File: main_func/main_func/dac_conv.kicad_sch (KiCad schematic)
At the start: 38 parts, among them U1 TXB0108PWR, U2 DRV603PW, U3 SN74AHC1G14DCKR, U4 PCM1753DBQR

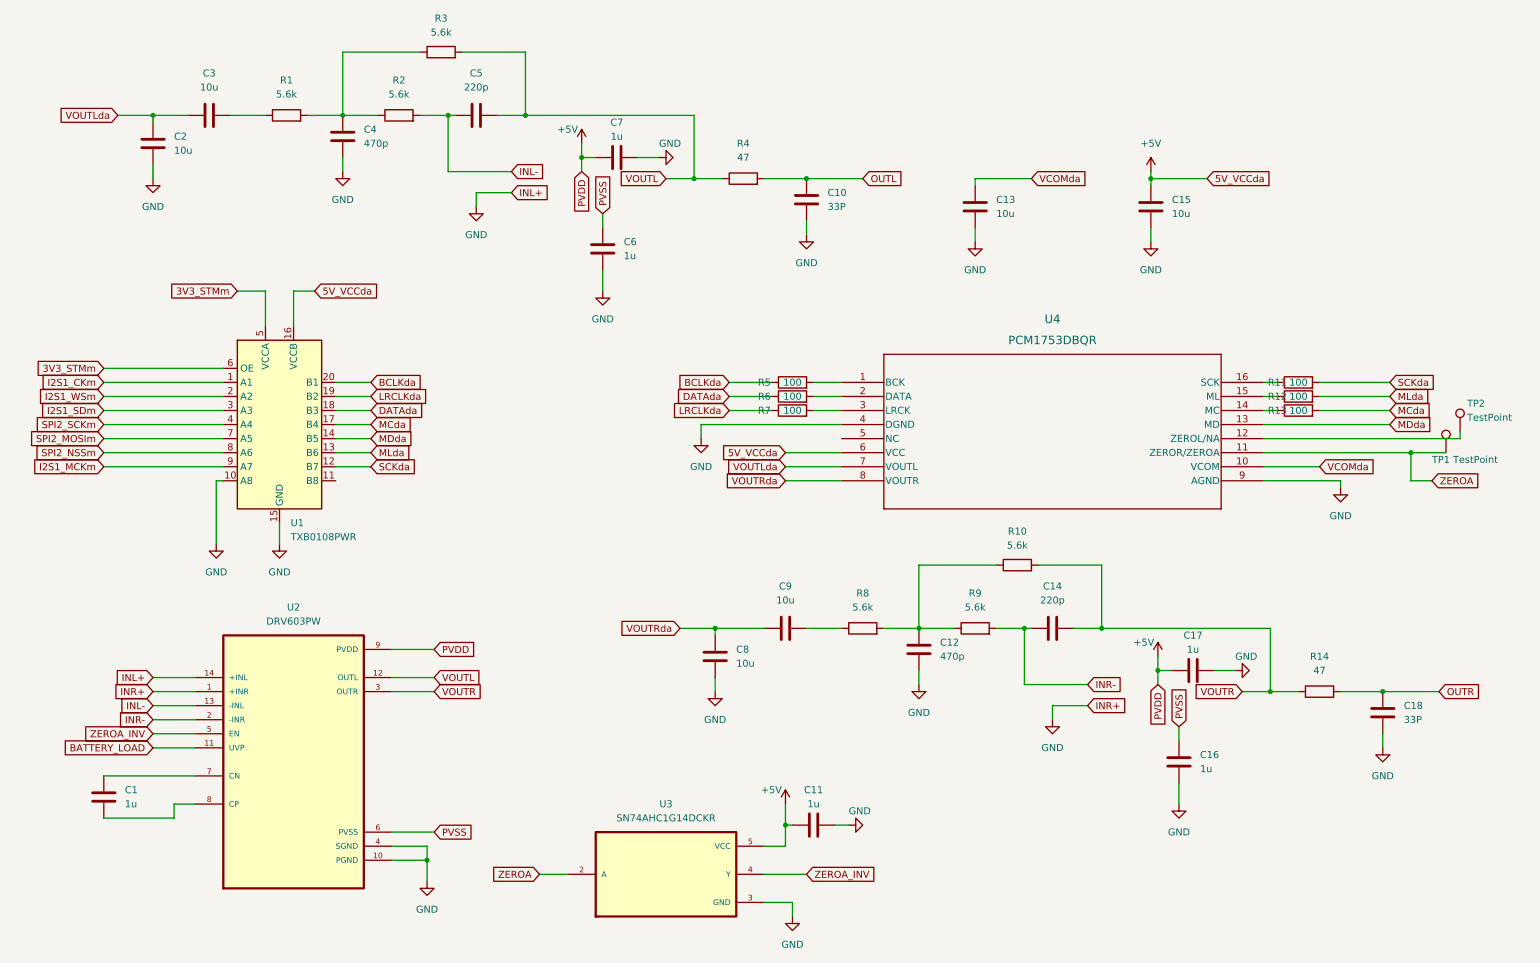
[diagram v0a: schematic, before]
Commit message: main func schematics fixed
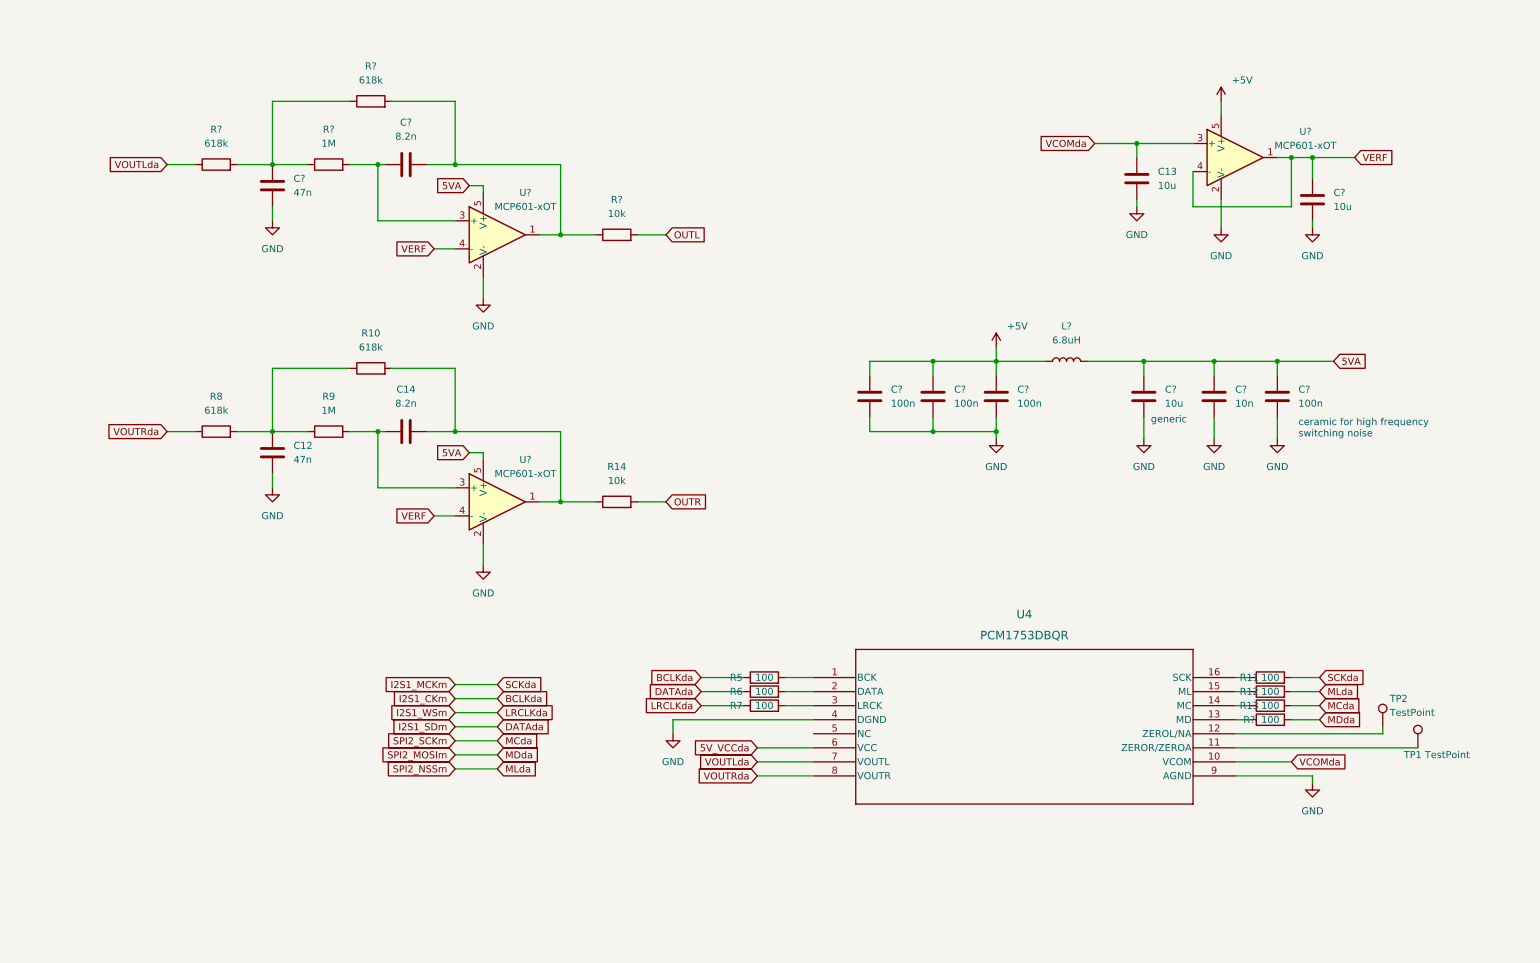
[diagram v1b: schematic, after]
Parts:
- removed C1, C11, C16, C17, C6, C7: 1u, Capacitor_SMD:C_0805_2012Metric_Pad1.18x1.45mm_HandSolder, symbol Device:C
- removed C10, C18: 33P, Capacitor_SMD:C_0805_2012Metric_Pad1.18x1.45mm_HandSolder, symbol Device:C
- removed C15, C2, C3, C8, C9: 10u, Capacitor_SMD:C_0805_2012Metric_Pad1.18x1.45mm_HandSolder, symbol Device:C
- removed C4: 470p, Capacitor_SMD:C_0805_2012Metric_Pad1.18x1.45mm_HandSolder, symbol Device:C
- removed C5: 220p, Capacitor_SMD:C_0805_2012Metric_Pad1.18x1.45mm_HandSolder, symbol Device:C
- removed R1, R2, R3: 5.6k, Resistor_SMD:R_0805_2012Metric_Pad1.20x1.40mm_HandSolder, symbol Device:R
- removed R4: 47, Resistor_SMD:R_0805_2012Metric_Pad1.20x1.40mm_HandSolder, symbol Device:R
- removed U1: TXB0108PWR, Package_SO:TSSOP-20_4.4x6.5mm_P0.65mm, symbol Logic_LevelTranslator:TXB0108DQSR
- removed U2: DRV603PW, DRV603PW:SOP65P640X120-14N, symbol DRV603PW:DRV603PW
- removed U3: SN74AHC1G14DCKR, SN74AHC1G14DCKR:SOT65P210X110-5N, symbol SN74AHC1G14DCKR:SN74AHC1G14DCKR
- added C?: 10n, Capacitor_SMD:C_0805_2012Metric_Pad1.18x1.45mm_HandSolder, symbol Device:C
- added C? (x4): 100n, Capacitor_SMD:C_0805_2012Metric_Pad1.18x1.45mm_HandSolder, symbol Device:C
- added C? (x2): 10u, Capacitor_SMD:C_0805_2012Metric_Pad1.18x1.45mm_HandSolder, symbol Device:C
- added C?: 47n, Capacitor_SMD:C_0805_2012Metric_Pad1.18x1.45mm_HandSolder, symbol Device:C
- added C?: 8.2n, Capacitor_SMD:C_0805_2012Metric_Pad1.18x1.45mm_HandSolder, symbol Device:C
- added L?: 6.8uH, inductors:inductor_koherelec, symbol Device:L
- added R?: 100, Resistor_SMD:R_0805_2012Metric_Pad1.20x1.40mm_HandSolder, symbol Device:R
- added R? (x2): 618k, Resistor_SMD:R_0805_2012Metric_Pad1.20x1.40mm_HandSolder, symbol Device:R
- added R?: 1M, Resistor_SMD:R_0805_2012Metric_Pad1.20x1.40mm_HandSolder, symbol Device:R
- added R?: 10k, Resistor_SMD:R_0805_2012Metric_Pad1.20x1.40mm_HandSolder, symbol Device:R
- added U? (x3): MCP601-xOT, Package_TO_SOT_SMD:SOT-23-5, symbol Amplifier_Operational:MCP601-xOT
- C12: value 470p -> 47n
- C14: value 220p -> 8.2n
- R10, R8: value 5.6k -> 618k
- R14: value 47 -> 10k
- R9: value 5.6k -> 1M
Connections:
- net LRCLKda is gone; now on net I2S1_WSm: R7.1
- net SCKda is gone; now on net I2S1_MCKm: R11.2
- net +5V: now also C?.1, C?.1, C?.1, L?.1, U?.5 (V+); no longer U4.6 (VCC)
- net GND: now also C?.2, C?.2, C?.2, C?.2, C?.2, C?.2, C?.2, C?.2, U?.2 (V-), U?.2 (V-), U?.2 (V-)
- net MDda: now also R?.2; no longer U4.13 (MD)
- net OUTL: now also R?.2
- net VCOMda: now also U?.3 (+)
- net VOUTLda: now also R?.1
- net VOUTRda: now also R8.1
- net INR-: no longer names the net of C14.1, R9.2
- net INR-: now also U?.3 (+)
- net VOUTR: no longer names the net of C14.2, R10.2, R14.1
- net VOUTR: now also U?.1
- net ZEROA: no longer names the net of TP1.1, U4.11 (ZEROR/ZEROA)
- new net: C?.2, R?.1, R?.2, U?.1
- new net: C?.1, R?.2, U?.3 (+)
- new net: R?.1, U4.13 (MD)
- new net: C?.1, R?.1, R?.1, R?.2
- new net 5VA: C?.1, C?.1, C?.1, L?.2, U?.5 (V+), U?.5 (V+)
- new net 5V_VCCda: U4.6 (VCC)
- new net VERF: C?.1, U?.1, U?.4 (-), U?.4 (-), U?.4 (-)
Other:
- note added: "ceramic for high frequency switching noise"
- note added: "generic"
- moved on the sheet: C12, C13, C14, R10, R11, R12, R13, R14, R5, R6, R7, R8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

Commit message: fixing keyboard and pot project schematics
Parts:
- gave numbers to parts that had none: 18
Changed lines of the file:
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@@
   (symbol (lib_id "Amplifier_Operational:MCP601-xOT") (at 100.33 49.53 0) (unit 1)
     (in_bom yes) (on_board yes)
-    (property "Reference" "U?" (id 0) (at 105.41 41.91 0))
+    (property "Reference" "U1" (id 0) (at 105.41 41.91 0))
     (property "Value" "MCP601-xOT" (id 1) (at 105.41 44.45 0))
     (property "Footprint" "Package_TO_SOT_SMD:SOT-23-5" (id 2) (at 97.79 54.61 0)
@@
   (symbol (lib_id "Device:C") (at 229.87 78.74 0) (unit 1)
     (in_bom yes) (on_board yes) (fields_autoplaced)
-    (property "Reference" "C?" (id 0) (at 233.68 77.4699 0)
+    (property "Reference" "C7" (id 0) (at 233.68 77.4699 0)
       (effects (font (size 1.27 1.27)) (justify left))
     )
@@
   (symbol (lib_id "Device:C") (at 241.3 78.74 0) (unit 1)
     (in_bom yes) (on_board yes) (fields_autoplaced)
-    (property "Reference" "C?" (id 0) (at 245.11 77.4699 0)
+    (property "Reference" "C8" (id 0) (at 245.11 77.4699 0)
       (effects (font (size 1.27 1.27)) (justify left))
     )
@@
   (symbol (lib_id "power:GND") (at 231.14 48.26 0) (unit 1)
     (in_bom yes) (on_board yes) (fields_autoplaced)
-    (property "Reference" "#PWR?" (id 0) (at 231.14 54.61 0)
+    (property "Reference" "#PWR08" (id 0) (at 231.14 54.61 0)
       (effects (font (size 1.27 1.27)) hide)
     )
@@
   (symbol (lib_id "Device:C") (at 217.17 78.74 0) (unit 1)
     (in_bom yes) (on_board yes) (fields_autoplaced)
-    (property "Reference" "C?" (id 0) (at 220.98 77.4699 0)
+    (property "Reference" "C6" (id 0) (at 220.98 77.4699 0)
       (effects (font (size 1.27 1.27)) (justify left))
     )
@@
   (symbol (lib_id "Device:R") (at 240.03 137.16 90) (unit 1)
     (in_bom yes) (on_board yes)
-    (property "Reference" "R?" (id 0) (at 236.22 137.16 90))
+    (property "Reference" "R28" (id 0) (at 236.22 137.16 90))
     (property "Value" "100" (id 1) (at 240.03 137.16 90))
     (property "Footprint" "Resistor_SMD:R_0805_2012Metric_Pad1.20x1.40mm_HandSolder" (id 2) (at 240.03 138.938 90)
@@
   (symbol (lib_id "power:GND") (at 247.65 48.26 0) (unit 1)
     (in_bom yes) (on_board yes) (fields_autoplaced)
-    (property "Reference" "#PWR?" (id 0) (at 247.65 54.61 0)
+    (property "Reference" "#PWR011" (id 0) (at 247.65 54.61 0)
       (effects (font (size 1.27 1.27)) hide)
     )
@@
   (symbol (lib_id "Device:C") (at 59.69 40.64 0) (unit 1)
     (in_bom yes) (on_board yes) (fields_autoplaced)
-    (property "Reference" "C?" (id 0) (at 63.5 39.3699 0)
+    (property "Reference" "C1" (id 0) (at 63.5 39.3699 0)
       (effects (font (size 1.27 1.27)) (justify left))
     )
@@
   (symbol (lib_id "power:GND") (at 217.17 86.36 0) (unit 1)
     (in_bom yes) (on_board yes) (fields_autoplaced)
-    (property "Reference" "#PWR?" (id 0) (at 217.17 92.71 0)
+    (property "Reference" "#PWR05" (id 0) (at 217.17 92.71 0)
       (effects (font (size 1.27 1.27)) hide)
     )
@@
   (symbol (lib_id "Device:C") (at 167.64 78.74 0) (unit 1)
     (in_bom yes) (on_board yes) (fields_autoplaced)
-    (property "Reference" "C?" (id 0) (at 171.45 77.4699 0)
+    (property "Reference" "C3" (id 0) (at 171.45 77.4699 0)
       (effects (font (size 1.27 1.27)) (justify left))
     )
@@
   (symbol (lib_id "power:GND") (at 59.69 46.99 0) (unit 1)
     (in_bom yes) (on_board yes) (fields_autoplaced)
-    (property "Reference" "#PWR?" (id 0) (at 59.69 53.34 0)
+    (property "Reference" "#PWR01" (id 0) (at 59.69 53.34 0)
       (effects (font (size 1.27 1.27)) hide)
     )
@@
   (symbol (lib_id "Device:C") (at 190.5 78.74 0) (unit 1)
     (in_bom yes) (on_board yes) (fields_autoplaced)
-    (property "Reference" "C?" (id 0) (at 194.31 77.4699 0)
+    (property "Reference" "C5" (id 0) (at 194.31 77.4699 0)
       (effects (font (size 1.27 1.27)) (justify left))
     )
@@
   (symbol (lib_id "power:GND") (at 190.5 86.36 0) (unit 1)
     (in_bom yes) (on_board yes) (fields_autoplaced)
-    (property "Reference" "#PWR?" (id 0) (at 190.5 92.71 0)
+    (property "Reference" "#PWR04" (id 0) (at 190.5 92.71 0)
       (effects (font (size 1.27 1.27)) hide)
     )
@@
   (symbol (lib_id "Amplifier_Operational:MCP601-xOT") (at 233.68 35.56 0) (unit 1)
     (in_bom yes) (on_board yes) (fields_autoplaced)
-    (property "Reference" "U?" (id 0) (at 246.38 30.861 0))
+    (property "Reference" "U3" (id 0) (at 246.38 30.861 0))
     (property "Value" "MCP601-xOT" (id 1) (at 246.38 33.401 0))
     (property "Footprint" "Package_TO_SOT_SMD:SOT-23-5" (id 2) (at 231.14 40.64 0)
@@
   (symbol (lib_id "Device:R") (at 77.47 25.4 90) (unit 1)
     (in_bom yes) (on_board yes) (fields_autoplaced)
-    (property "Reference" "R?" (id 0) (at 77.47 19.05 90))
+    (property "Reference" "R3" (id 0) (at 77.47 19.05 90))
     (property "Value" "618k" (id 1) (at 77.47 21.59 90))
     (property "Footprint" "Resistor_SMD:R_0805_2012Metric_Pad1.20x1.40mm_HandSolder" (id 2) (at 77.47 27.178 90)
@@
   (symbol (lib_id "power:GND") (at 241.3 86.36 0) (unit 1)
     (in_bom yes) (on_board yes) (fields_autoplaced)
-    (property "Reference" "#PWR?" (id 0) (at 241.3 92.71 0)
+    (property "Reference" "#PWR09" (id 0) (at 241.3 92.71 0)
       (effects (font (size 1.27 1.27)) hide)
     )
@@
   (symbol (lib_id "power:+5V") (at 231.14 25.4 0) (unit 1)
     (in_bom yes) (on_board yes)
-    (property "Reference" "#PWR?" (id 0) (at 231.14 29.21 0)
+    (property "Reference" "#PWR07" (id 0) (at 231.14 29.21 0)
       (effects (font (size 1.27 1.27)) hide)
     )
@@
   (symbol (lib_id "Device:R") (at 49.53 36.83 90) (unit 1)
     (in_bom yes) (on_board yes) (fields_autoplaced)
-    (property "Reference" "R?" (id 0) (at 49.53 30.48 90))
+    (property "Reference" "R1" (id 0) (at 49.53 30.48 90))
     (property "Value" "618k" (id 1) (at 49.53 33.02 90))
     (property "Footprint" "Resistor_SMD:R_0805_2012Metric_Pad1.20x1.40mm_HandSolder" (id 2) (at 49.53 38.608 90)
@@
   (symbol (lib_id "Device:C") (at 179.07 78.74 0) (unit 1)
     (in_bom yes) (on_board yes) (fields_autoplaced)
-    (property "Reference" "C?" (id 0) (at 182.88 77.4699 0)
+    (property "Reference" "C4" (id 0) (at 182.88 77.4699 0)
       (effects (font (size 1.27 1.27)) (justify left))
     )
@@
   (symbol (lib_id "Device:C") (at 83.82 36.83 90) (unit 1)
     (in_bom yes) (on_board yes) (fields_autoplaced)
-    (property "Reference" "C?" (id 0) (at 83.82 29.21 90))
+    (property "Reference" "C2" (id 0) (at 83.82 29.21 90))
     (property "Value" "8.2n" (id 1) (at 83.82 31.75 90))
     (property "Footprint" "Capacitor_SMD:C_0805_2012Metric_Pad1.18x1.45mm_HandSolder" (id 2) (at 87.63 35.8648 0)
@@
   (symbol (lib_id "Amplifier_Operational:MCP601-xOT") (at 100.33 97.79 0) (unit 1)
     (in_bom yes) (on_board yes)
-    (property "Reference" "U?" (id 0) (at 105.41 90.17 0))
+    (property "Reference" "U2" (id 0) (at 105.41 90.17 0))
     (property "Value" "MCP601-xOT" (id 1) (at 105.41 92.71 0))
     (property "Footprint" "Package_TO_SOT_SMD:SOT-23-5" (id 2) (at 97.79 102.87 0)
@@
   (symbol (lib_id "power:+5V") (at 190.5 69.85 0) (unit 1)
     (in_bom yes) (on_board yes)
-    (property "Reference" "#PWR?" (id 0) (at 190.5 73.66 0)
+    (property "Reference" "#PWR03" (id 0) (at 190.5 73.66 0)
       (effects (font (size 1.27 1.27)) hide)
     )
@@
   (symbol (lib_id "Device:L") (at 203.2 72.39 90) (unit 1)
     (in_bom yes) (on_board yes) (fields_autoplaced)
-    (property "Reference" "L?" (id 0) (at 203.2 66.04 90))
+    (property "Reference" "L1" (id 0) (at 203.2 66.04 90))
     (property "Value" "6.8uH" (id 1) (at 203.2 68.58 90))
     (property "Footprint" "inductors:inductor_koherelec" (id 2) (at 203.2 72.39 0)
@@
   (symbol (lib_id "Device:R") (at 69.85 36.83 90) (unit 1)
     (in_bom yes) (on_board yes) (fields_autoplaced)
-    (property "Reference" "R?" (id 0) (at 69.85 30.48 90))
+    (property "Reference" "R2" (id 0) (at 69.85 30.48 90))
     (property "Value" "1M" (id 1) (at 69.85 33.02 90))
     (property "Footprint" "Resistor_SMD:R_0805_2012Metric_Pad1.20x1.40mm_HandSolder" (id 2) (at 69.85 38.608 90)
@@
   (symbol (lib_id "power:GND") (at 229.87 86.36 0) (unit 1)
     (in_bom yes) (on_board yes) (fields_autoplaced)
-    (property "Reference" "#PWR?" (id 0) (at 229.87 92.71 0)
+    (property "Reference" "#PWR06" (id 0) (at 229.87 92.71 0)
       (effects (font (size 1.27 1.27)) hide)
     )
@@
   (symbol (lib_id "power:GND") (at 97.79 60.96 0) (unit 1)
     (in_bom yes) (on_board yes) (fields_autoplaced)
-    (property "Reference" "#PWR?" (id 0) (at 97.79 67.31 0)
+    (property "Reference" "#PWR02" (id 0) (at 97.79 67.31 0)
       (effects (font (size 1.27 1.27)) hide)
     )
@@
   (symbol (lib_id "Device:C") (at 247.65 43.18 0) (unit 1)
     (in_bom yes) (on_board yes) (fields_autoplaced)
-    (property "Reference" "C?" (id 0) (at 251.46 41.9099 0)
+    (property "Reference" "C9" (id 0) (at 251.46 41.9099 0)
       (effects (font (size 1.27 1.27)) (justify left))
     )
@@
   (symbol (lib_id "Device:R") (at 121.92 49.53 90) (unit 1)
     (in_bom yes) (on_board yes) (fields_autoplaced)
-    (property "Reference" "R?" (id 0) (at 121.92 43.18 90))
+    (property "Reference" "R4" (id 0) (at 121.92 43.18 90))
     (property "Value" "10k" (id 1) (at 121.92 45.72 90))
     (property "Footprint" "Resistor_SMD:R_0805_2012Metric_Pad1.20x1.40mm_HandSolder" (id 2) (at 121.92 51.308 90)
